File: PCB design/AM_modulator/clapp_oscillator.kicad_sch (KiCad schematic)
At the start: 11 parts, among them Q1 MMBT3904

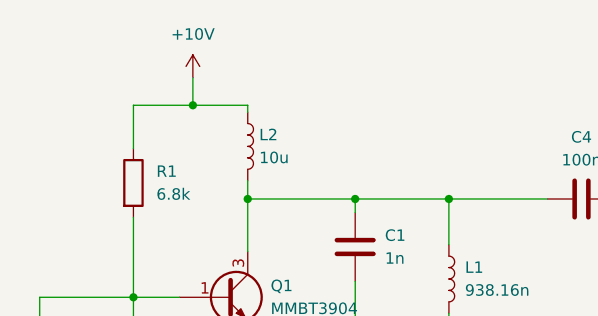
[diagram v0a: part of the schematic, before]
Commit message: Mixer en la placa
Integración del mezclador en la placa
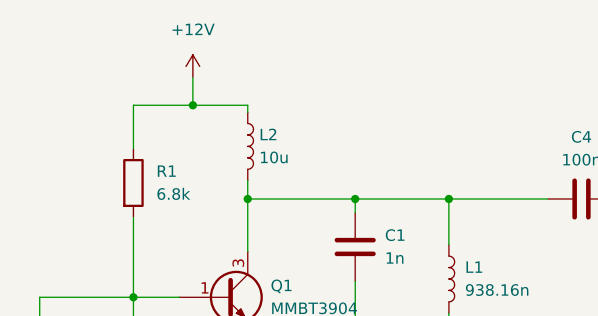
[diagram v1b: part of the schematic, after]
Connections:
- net +10V renamed +12V
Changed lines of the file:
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@@
     (effects (font (size 1.27 1.27)) (justify left))
+  )
+  (symbol (lib_id "power:+12V") (at 67.056 47.244 0) (unit 1)
+    (in_bom yes) (on_board yes) (fields_autoplaced)
+    (property "Reference" "#PWR0107" (id 0) (at 67.056 51.054 0)
+      (effects (font (size 1.27 1.27)) hide)
+    )
+    (property "Value" "+12V" (id 1) (at 67.056 41.91 0))
+    (property "Footprint" "" (id 2) (at 67.056 47.244 0)
+      (effects (font (size 1.27 1.27)) hide)
+    )
+    (property "Datasheet" "" (id 3) (at 67.056 47.244 0)
+      (effects (font (size 1.27 1.27)) hide)
+    )
+    (pin "1")
   )
   (symbol (lib_id "power:GND") (at 95.504 97.028 0) (unit 1)
@@
     (pin "2")
   )
-  (symbol (lib_id "power:+10V") (at 67.056 47.244 0) (unit 1)
-    (in_bom yes) (on_board yes) (fields_autoplaced)
-    (property "Reference" "#PWR0104" (id 0) (at 67.056 51.054 0)
-      (effects (font (size 1.27 1.27)) hide)
-    )
-    (property "Value" "+10V" (id 1) (at 67.056 42.418 0))
-    (property "Footprint" "" (id 2) (at 67.056 47.244 0)
-      (effects (font (size 1.27 1.27)) hide)
-    )
-    (property "Datasheet" "" (id 3) (at 67.056 47.244 0)
-      (effects (font (size 1.27 1.27)) hide)
-    )
-    (pin "1")
-  )
   (symbol (lib_id "Device:C") (at 110.236 60.706 90) (unit 1)

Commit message: Avances placa
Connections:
- net +12V: no longer R1.1
- net at C1.1, C4.1, L1.1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: now also R1.1
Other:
- moved on the sheet: R1
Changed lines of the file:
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@@
 (kicad_sch (version 20211123) (generator eeschema)
   (paper "User" 170.002 170.002)
-  (junction (at 67.056 50.292) (diameter 0) (color 0 0 0 0)
-  )
   (junction (at 73.152 78.232) (diameter 0) (color 0 0 0 0)
   )
@@
   )
   (wire (pts (xy 73.152 88.392) (xy 73.152 97.028))
-    (stroke (width 0) (type default) (color 0 0 0 0))
-  )
-  (wire (pts (xy 73.152 50.292) (xy 67.056 50.292))
     (stroke (width 0) (type default) (color 0 0 0 0))
   )
@@
     (stroke (width 0) (type default) (color 0 0 0 0))
   )
-  (wire (pts (xy 60.452 62.738) (xy 60.452 71.628))
+  (wire (pts (xy 60.452 70.104) (xy 60.452 71.628))
     (stroke (width 0) (type default) (color 0 0 0 0))
   )
@@
     (stroke (width 0) (type default) (color 0 0 0 0))
   )
-  (wire (pts (xy 67.056 50.292) (xy 60.452 50.292))
+  (wire (pts (xy 60.452 60.706) (xy 73.152 60.706))
     (stroke (width 0) (type default) (color 0 0 0 0))
   )
@@
   )
   (wire (pts (xy 85.09 69.85) (xy 85.09 78.232))
-    (stroke (width 0) (type default) (color 0 0 0 0))
-  )
-  (wire (pts (xy 67.056 47.244) (xy 67.056 50.292))
     (stroke (width 0) (type default) (color 0 0 0 0))
   )
@@
     (stroke (width 0) (type default) (color 0 0 0 0))
   )
-  (wire (pts (xy 73.152 51.054) (xy 73.152 50.292))
+  (wire (pts (xy 73.152 47.498) (xy 73.152 51.054))
+    (stroke (width 0) (type default) (color 0 0 0 0))
+  )
+  (wire (pts (xy 60.452 60.706) (xy 60.452 62.484))
     (stroke (width 0) (type default) (color 0 0 0 0))
   )
@@
     (stroke (width 0) (type default) (color 0 0 0 0))
   )
-  (wire (pts (xy 60.452 50.292) (xy 60.452 55.118))
-    (stroke (width 0) (type default) (color 0 0 0 0))
-  )
   (hierarchical_label "Vout_30MHz_50Ohm" (shape output) (at 120.396 60.706 0)
     (effects (font (size 1.27 1.27)) (justify left))
   )
-  (symbol (lib_id "power:+12V") (at 67.056 47.244 0) (unit 1)
+  (symbol (lib_id "power:+12V") (at 73.152 47.498 0) (unit 1)
     (in_bom yes) (on_board yes) (fields_autoplaced)
-    (property "Reference" "#PWR0107" (id 0) (at 67.056 51.054 0)
+    (property "Reference" "#PWR0107" (id 0) (at 73.152 51.308 0)
       (effects (font (size 1.27 1.27)) hide)
     )
-    (property "Value" "+12V" (id 1) (at 67.056 41.91 0))
-    (property "Footprint" "" (id 2) (at 67.056 47.244 0)
+    (property "Value" "+12V" (id 1) (at 73.152 42.164 0))
+    (property "Footprint" "" (id 2) (at 73.152 47.498 0)
       (effects (font (size 1.27 1.27)) hide)
     )
-    (property "Datasheet" "" (id 3) (at 67.056 47.244 0)
+    (property "Datasheet" "" (id 3) (at 73.152 47.498 0)
       (effects (font (size 1.27 1.27)) hide)
     )
@@
     (pin "1")
   )
-  (symbol (lib_id "Device:R") (at 60.452 58.928 0) (unit 1)
+  (symbol (lib_id "Device:R") (at 60.452 66.294 0) (unit 1)
     (in_bom yes) (on_board yes) (fields_autoplaced)
-    (property "Reference" "R1" (id 0) (at 62.992 57.6579 0)
+    (property "Reference" "R1" (id 0) (at 62.992 65.0239 0)
       (effects (font (size 1.27 1.27)) (justify left))
     )
-    (property "Value" "6.8k" (id 1) (at 62.992 60.1979 0)
+    (property "Value" "6.8k" (id 1) (at 62.992 67.5639 0)
       (effects (font (size 1.27 1.27)) (justify left))
     )
-    (property "Footprint" "Resistor_SMD:R_1206_3216Metric_Pad1.30x1.75mm_HandSolder" (id 2) (at 58.674 58.928 90)
+    (property "Footprint" "Resistor_SMD:R_1206_3216Metric_Pad1.30x1.75mm_HandSolder" (id 2) (at 58.674 66.294 90)
       (effects (font (size 1.27 1.27)) hide)
     )
-    (property "Datasheet" "~" (id 3) (at 60.452 58.928 0)
+    (property "Datasheet" "~" (id 3) (at 60.452 66.294 0)
       (effects (font (size 1.27 1.27)) hide)
     )

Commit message: Placa terminada
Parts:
- added J?: SMA_CONNECTOR, LPRS_SMA_CONNECTOR, symbol SMA_T:SMA_CONNECTOR
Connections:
- net GND: now also J?.G1, J?.G2, J?.G3, J?.G4
- net Vout_30MHz_50Ohm: now also J?.1
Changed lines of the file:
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@@
 (kicad_sch (version 20211123) (generator eeschema)
   (paper "User" 170.002 170.002)
+  (junction (at 118.872 60.706) (diameter 0) (color 0 0 0 0)
+  )
   (junction (at 73.152 78.232) (diameter 0) (color 0 0 0 0)
   )
@@
     (stroke (width 0) (type default) (color 0 0 0 0))
   )
+  (wire (pts (xy 118.872 66.294) (xy 117.856 66.294))
+    (stroke (width 0) (type default) (color 0 0 0 0))
+  )
   (wire (pts (xy 50.038 88.392) (xy 50.038 97.028))
     (stroke (width 0) (type default) (color 0 0 0 0))
@@
     (stroke (width 0) (type default) (color 0 0 0 0))
   )
-  (wire (pts (xy 114.046 60.706) (xy 120.396 60.706))
+  (wire (pts (xy 114.046 60.706) (xy 118.872 60.706))
     (stroke (width 0) (type default) (color 0 0 0 0))
   )
@@
     (stroke (width 0) (type default) (color 0 0 0 0))
   )
+  (wire (pts (xy 117.856 68.834) (xy 118.872 68.834))
+    (stroke (width 0) (type default) (color 0 0 0 0))
+  )
   (wire (pts (xy 60.452 60.706) (xy 73.152 60.706))
     (stroke (width 0) (type default) (color 0 0 0 0))
@@
     (stroke (width 0) (type default) (color 0 0 0 0))
   )
+  (wire (pts (xy 118.872 60.706) (xy 120.396 60.706))
+    (stroke (width 0) (type default) (color 0 0 0 0))
+  )
   (wire (pts (xy 85.09 78.232) (xy 85.09 81.788))
     (stroke (width 0) (type default) (color 0 0 0 0))
@@
   )
   (wire (pts (xy 50.038 80.772) (xy 50.038 71.628))
+    (stroke (width 0) (type default) (color 0 0 0 0))
+  )
+  (wire (pts (xy 118.872 60.706) (xy 118.872 66.294))
     (stroke (width 0) (type default) (color 0 0 0 0))
   )
@@
     (pin "2")
   )
+  (symbol (lib_id "power:GND") (at 118.872 68.834 0) (unit 1)
+    (in_bom yes) (on_board yes) (fields_autoplaced)
+    (property "Reference" "#PWR0116" (id 0) (at 118.872 75.184 0)
+      (effects (font (size 1.27 1.27)) hide)
+    )
+    (property "Value" "GND" (id 1) (at 118.872 73.66 0))
+    (property "Footprint" "" (id 2) (at 118.872 68.834 0)
+      (effects (font (size 1.27 1.27)) hide)
+    )
+    (property "Datasheet" "" (id 3) (at 118.872 68.834 0)
+      (effects (font (size 1.27 1.27)) hide)
+    )
+    (pin "1")
+  )
+  (symbol (lib_id "SMA_T:SMA_CONNECTOR") (at 115.316 66.294 0) (unit 1)
+    (in_bom yes) (on_board yes)
+    (property "Reference" "J?" (id 0) (at 120.904 66.294 0))
+    (property "Value" "SMA_CONNECTOR" (id 1) (at 127.762 68.58 0))
+    (property "Footprint" "LPRS_SMA_CONNECTOR" (id 2) (at 115.316 66.294 0)
+      (effects (font (size 1.27 1.27)) (justify left bottom) hide)
+    )
+    (property "Datasheet" "" (id 3) (at 115.316 66.294 0)
+      (effects (font (size 1.27 1.27)) (justify left bottom) hide)
+    )
+    (property "MANUFACTURER" "LPRS" (id 4) (at 115.316 66.294 0)
+      (effects (font (size 1.27 1.27)) (justify left bottom) hide)
+    )
+    (property "MAXIMUM_PACKAGE_HEIGHT" "8.3 mm" (id 5) (at 115.316 66.294 0)
+      (effects (font (size 1.27 1.27)) (justify left bottom) hide)
+    )
+    (property "STANDARD" "Manufacturer Recommendations" (id 6) (at 115.316 66.294 0)
+      (effects (font (size 1.27 1.27)) (justify left bottom) hide)
+    )
+    (property "PARTREV" "1.3" (id 7) (at 115.316 66.294 0)
+      (effects (font (size 1.27 1.27)) (justify left bottom) hide)
+    )
+    (pin "1")
+    (pin "G1")
+    (pin "G2")
+    (pin "G3")
+    (pin "G4")
+  )
   (symbol (lib_id "power:GND") (at 50.038 97.028 0) (unit 1)

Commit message: PCB 2.0
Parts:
- added SW3: SW_DIP_x01, Resistor_SMD:R_0603_1608Metric_Pad0.98x0.95mm_HandSolder, symbol Switch:SW_DIP_x01
- J3: renamed from J?; footprint LPRS_SMA_CONNECTOR -> SMA_T:LPRS_SMA_CONNECTOR
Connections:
- net Vout_30MHz_50Ohm: now also SW3.2; no longer C4.2
- new net: C4.2, SW3.1
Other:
- moved on the sheet: J3
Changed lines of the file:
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@@
 (kicad_sch (version 20211123) (generator eeschema)
   (paper "User" 170.002 170.002)
-  (junction (at 118.872 60.706) (diameter 0) (color 0 0 0 0)
+  (junction (at 146.304 60.706) (diameter 0) (color 0 0 0 0)
   )
   (junction (at 73.152 78.232) (diameter 0) (color 0 0 0 0)
@@
     (stroke (width 0) (type default) (color 0 0 0 0))
   )
-  (wire (pts (xy 118.872 66.294) (xy 117.856 66.294))
+  (wire (pts (xy 146.304 66.294) (xy 145.288 66.294))
     (stroke (width 0) (type default) (color 0 0 0 0))
   )
@@
     (stroke (width 0) (type default) (color 0 0 0 0))
   )
-  (wire (pts (xy 114.046 60.706) (xy 118.872 60.706))
+  (wire (pts (xy 114.046 60.706) (xy 121.158 60.706))
     (stroke (width 0) (type default) (color 0 0 0 0))
   )
@@
     (stroke (width 0) (type default) (color 0 0 0 0))
   )
-  (wire (pts (xy 117.856 68.834) (xy 118.872 68.834))
+  (wire (pts (xy 145.288 68.834) (xy 146.304 68.834))
     (stroke (width 0) (type default) (color 0 0 0 0))
   )
@@
     (stroke (width 0) (type default) (color 0 0 0 0))
   )
-  (wire (pts (xy 118.872 60.706) (xy 120.396 60.706))
+  (wire (pts (xy 146.304 60.706) (xy 147.828 60.706))
     (stroke (width 0) (type default) (color 0 0 0 0))
   )
@@
     (stroke (width 0) (type default) (color 0 0 0 0))
   )
-  (wire (pts (xy 118.872 60.706) (xy 118.872 66.294))
+  (wire (pts (xy 146.304 60.706) (xy 146.304 66.294))
     (stroke (width 0) (type default) (color 0 0 0 0))
   )
@@
     (stroke (width 0) (type default) (color 0 0 0 0))
   )
+  (wire (pts (xy 136.398 60.706) (xy 146.304 60.706))
+    (stroke (width 0) (type default) (color 0 0 0 0))
+  )
   (wire (pts (xy 95.504 60.706) (xy 106.426 60.706))
     (stroke (width 0) (type default) (color 0 0 0 0))
@@
     (stroke (width 0) (type default) (color 0 0 0 0))
   )
-  (hierarchical_label "Vout_30MHz_50Ohm" (shape output) (at 120.396 60.706 0)
+  (hierarchical_label "Vout_30MHz_50Ohm" (shape output) (at 147.828 60.706 0)
     (effects (font (size 1.27 1.27)) (justify left))
   )
@@
     (pin "1")
   )
+  (symbol (lib_id "Switch:SW_DIP_x01") (at 128.778 60.706 0) (unit 1)
+    (in_bom yes) (on_board yes) (fields_autoplaced)
+    (property "Reference" "SW3" (id 0) (at 128.778 53.34 0))
+    (property "Value" "SW_DIP_x01" (id 1) (at 128.778 55.88 0))
+    (property "Footprint" "Resistor_SMD:R_0603_1608Metric_Pad0.98x0.95mm_HandSolder" (id 2) (at 128.778 60.706 0)
+      (effects (font (size 1.27 1.27)) hide)
+    )
+    (property "Datasheet" "~" (id 3) (at 128.778 60.706 0)
+      (effects (font (size 1.27 1.27)) hide)
+    )
+    (pin "1")
+    (pin "2")
+  )
   (symbol (lib_id "power:GND") (at 95.504 97.028 0) (unit 1)
     (in_bom yes) (on_board yes) (fields_autoplaced)
@@
     (pin "2")
   )
-  (symbol (lib_id "power:GND") (at 118.872 68.834 0) (unit 1)
-    (in_bom yes) (on_board yes) (fields_autoplaced)
-    (property "Reference" "#PWR0116" (id 0) (at 118.872 75.184 0)
-      (effects (font (size 1.27 1.27)) hide)
-    )
-    (property "Value" "GND" (id 1) (at 118.872 73.66 0))
-    (property "Footprint" "" (id 2) (at 118.872 68.834 0)
-      (effects (font (size 1.27 1.27)) hide)
-    )
-    (property "Datasheet" "" (id 3) (at 118.872 68.834 0)
-      (effects (font (size 1.27 1.27)) hide)
-    )
-    (pin "1")
-  )
-  (symbol (lib_id "SMA_T:SMA_CONNECTOR") (at 115.316 66.294 0) (unit 1)
+  (symbol (lib_id "power:GND") (at 146.304 68.834 0) (unit 1)
+    (in_bom yes) (on_board yes) (fields_autoplaced)
+    (property "Reference" "#PWR0116" (id 0) (at 146.304 75.184 0)
+      (effects (font (size 1.27 1.27)) hide)
+    )
+    (property "Value" "GND" (id 1) (at 146.304 73.66 0))
+    (property "Footprint" "" (id 2) (at 146.304 68.834 0)
+      (effects (font (size 1.27 1.27)) hide)
+    )
+    (property "Datasheet" "" (id 3) (at 146.304 68.834 0)
+      (effects (font (size 1.27 1.27)) hide)
+    )
+    (pin "1")
+  )
+  (symbol (lib_id "SMA_T:SMA_CONNECTOR") (at 142.748 66.294 0) (unit 1)
     (in_bom yes) (on_board yes)
-    (property "Reference" "J?" (id 0) (at 120.904 66.294 0))
-    (property "Value" "SMA_CONNECTOR" (id 1) (at 127.762 68.58 0))
-    (property "Footprint" "LPRS_SMA_CONNECTOR" (id 2) (at 115.316 66.294 0)
-      (effects (font (size 1.27 1.27)) (justify left bottom) hide)
-    )
-    (property "Datasheet" "" (id 3) (at 115.316 66.294 0)
-      (effects (font (size 1.27 1.27)) (justify left bottom) hide)
-    )
-    (property "MANUFACTURER" "LPRS" (id 4) (at 115.316 66.294 0)
-      (effects (font (size 1.27 1.27)) (justify left bottom) hide)
-    )
-    (property "MAXIMUM_PACKAGE_HEIGHT" "8.3 mm" (id 5) (at 115.316 66.294 0)
-      (effects (font (size 1.27 1.27)) (justify left bottom) hide)
-    )
-    (property "STANDARD" "Manufacturer Recommendations" (id 6) (at 115.316 66.294 0)
-      (effects (font (size 1.27 1.27)) (justify left bottom) hide)
-    )
-    (property "PARTREV" "1.3" (id 7) (at 115.316 66.294 0)
-      (effects (font (size 1.27 1.27)) (justify left bottom) hide)
-    )
+    (property "Reference" "J3" (id 0) (at 148.336 66.294 0))
+    (property "Value" "SMA_CONNECTOR" (id 1) (at 155.194 68.58 0))
+    (property "Footprint" "SMA_T:LPRS_SMA_CONNECTOR" (id 2) (at 142.748 66.294 0)
+      (effects (font (size 1.27 1.27)) (justify left bottom) hide)
+    )
+    (property "Datasheet" "" (id 3) (at 142.748 66.294 0)
+      (effects (font (size 1.27 1.27)) (justify left bottom) hide)
+    )
+    (property "MANUFACTURER" "LPRS" (id 4) (at 142.748 66.294 0)
+      (effects (font (size 1.27 1.27)) (justify left bottom) hide)
+    )
+    (property "MAXIMUM_PACKAGE_HEIGHT" "8.3 mm" (id 5) (at 142.748 66.294 0)
+      (effects (font (size 1.27 1.27)) (justify left bottom) hide)
+    )
+    (property "STANDARD" "Manufacturer Recommendations" (id 6) (at 142.748 66.294 0)
+      (effects (font (size 1.27 1.27)) (justify left bottom) hide)
+    )
+    (property "PARTREV" "1.3" (id 7) (at 142.748 66.294 0)
+      (effects (font (size 1.27 1.27)) (justify left bottom) hide)
+    )

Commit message: PCB design done
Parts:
- removed Cv1: 30p, capacitors:variable_cap, symbol Device:C_Variable
- removed J3: SMA_CONNECTOR, SMA_T:LPRS_SMA_CONNECTOR, symbol SMA_T:SMA_CONNECTOR
- removed L1: 938.16n, inductors:air_core_1cm, symbol Device:L
- removed L2: 10u, inductors:T-130, symbol Device:L
- removed SW3: SW_DIP_x01, Resistor_SMD:R_0603_1608Metric_Pad0.98x0.95mm_HandSolder, symbol Switch:SW_DIP_x01
- added C5: 100n, Capacitor_SMD:C_0805_2012Metric_Pad1.18x1.45mm_HandSolder, symbol Device:C
- added L1: 250n, inductors:air_core_1cm, symbol Device:L_Trim
- C1: value 1n -> 220p
- C2: value 10n -> 220p
- R1: value 6.8k -> 10k
- R2: value 3.3k -> 15k
- R3: value 68 -> 470
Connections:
- net +12V: now also R1.1, C5.2
- net GND: now also C5.1; no longer C2.2
- net Vout_30MHz_50Ohm: now also C4.2
- net at C1.1, C4.1, Q1.3 (C): now also L1.1; no longer R1.1
- new net: C2.2, L1.2
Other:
- moved on the sheet: C1, C2

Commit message: PCB design done
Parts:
- L1: footprint inductors:air_core_1cm -> inductors:variable_inductor
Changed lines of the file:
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@@
       (effects (font (size 1.27 1.27)) (justify left))
     )
-    (property "Footprint" "inductors:air_core_1cm" (id 2) (at 95.504 75.946 0)
+    (property "Footprint" "inductors:variable_inductor" (id 2) (at 95.504 75.946 0)
       (effects (font (size 1.27 1.27)) hide)
     )

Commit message: PCB design done
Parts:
- R3: value 470 -> 430
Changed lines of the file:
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@@
       (effects (font (size 1.27 1.27)) (justify left))
     )
-    (property "Value" "470" (id 1) (at 74.93 85.8519 0)
+    (property "Value" "430" (id 1) (at 74.93 85.8519 0)
       (effects (font (size 1.27 1.27)) (justify left))
     )

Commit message: PCB corregida
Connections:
- net +12V: now also C2.2, L1.2
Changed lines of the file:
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@@
 (kicad_sch (version 20211123) (generator eeschema)
   (paper "User" 170.002 170.002)
+  (junction (at 95.504 89.916) (diameter 0) (color 0 0 0 0)
+  )
   (junction (at 73.152 78.232) (diameter 0) (color 0 0 0 0)
   )
@@
   (junction (at 60.452 71.628) (diameter 0) (color 0 0 0 0)
   )
+  (junction (at 95.504 95.504) (diameter 0) (color 0 0 0 0)
+  )
   (junction (at 85.09 60.706) (diameter 0) (color 0 0 0 0)
+  )
+  (wire (pts (xy 95.504 95.504) (xy 106.68 95.504))
+    (stroke (width 0) (type default) (color 0 0 0 0))
   )
   (wire (pts (xy 73.152 88.392) (xy 73.152 95.504))
@@
     (stroke (width 0) (type default) (color 0 0 0 0))
   )
+  (wire (pts (xy 95.504 89.916) (xy 95.504 95.504))
+    (stroke (width 0) (type default) (color 0 0 0 0))
+  )
   (wire (pts (xy 60.452 71.628) (xy 65.532 71.628))
     (stroke (width 0) (type default) (color 0 0 0 0))
@@
     (stroke (width 0) (type default) (color 0 0 0 0))
   )
-  (wire (pts (xy 93.472 95.504) (xy 106.68 95.504))
+  (wire (pts (xy 93.472 95.504) (xy 95.504 95.504))
     (stroke (width 0) (type default) (color 0 0 0 0))
   )
